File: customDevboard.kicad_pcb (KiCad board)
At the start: 4 copper layers, 40 x 40 mm, 110 parts, among them J1 Conn_01x01, J10 Conn_01x01, J11 Conn_01x01, J12 Conn_01x01, J13 Conn_01x01, J14 Conn_01x01, J15 Conn_01x01, J16 Conn_01x01, J17 Conn_01x01, J18 Conn_01x01, J19 Conn_01x01, J2 USB_C_Receptacle_USB2.0_14P, J20 From BEC, J21 Conn_01x01, J22 Conn_01x01, J23 Conn_01x01, J24 Conn_01x01, J25 PA0, J26 PA1, J27 PA7, J28 PA6, J29 PA5, J3 Conn_01x01, J30 PC1, J31 PC11, J32 PB13, J33 PA4, J34 PB2, J35 PC11, J36 PC10, J37 PB6, J38 PB7, J39 PA9, J4 Conn_01x01, J40 PA10, J41 PA2, J42 PA3, J43 PB10, J44 PB11, J5 Conn_01x01, J6 Debug, J7 To GPS, J8 BZ+, J9 COL, Q1 BC817, Q2 AO3401A, SW1 CK_KMS2xxGP, SW2 CK_KMS2xxGP, U1 DPS310, U3 TPD2EUSB30, U5 STM32F722RET6, U6 TLV75733PDRV, U7 BMI270, Y1 32.768KHz, Y2 8Mhz

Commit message: add buttons and fix drc
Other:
- board text removed: "RST"
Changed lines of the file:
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@@
-		)
-	)
-	(gr_text "RST"
-		(at 58 45 0)
-		(layer "F.SilkS")
-		(effects
-			(font
-				(size 1.5 1.5)
-				(thickness 0.3)
-				(bold yes)
-			)
-			(justify left bottom)
 		)
 	)

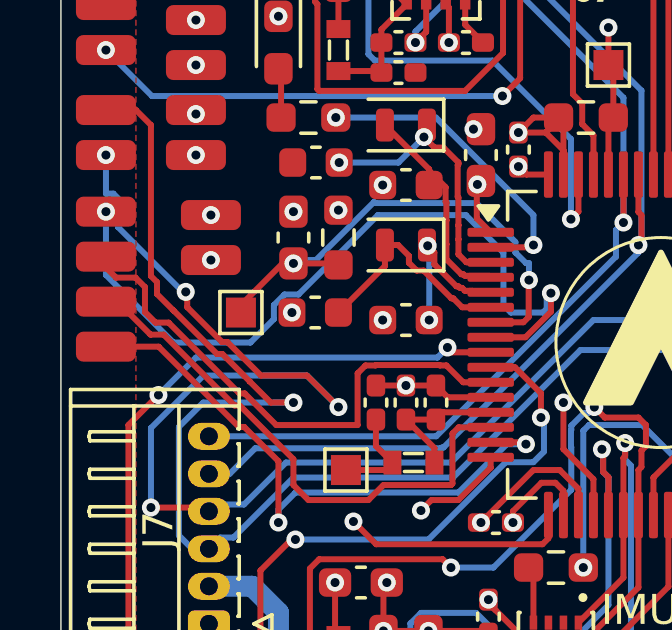
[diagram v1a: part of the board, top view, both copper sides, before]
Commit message: switch imu and barometer
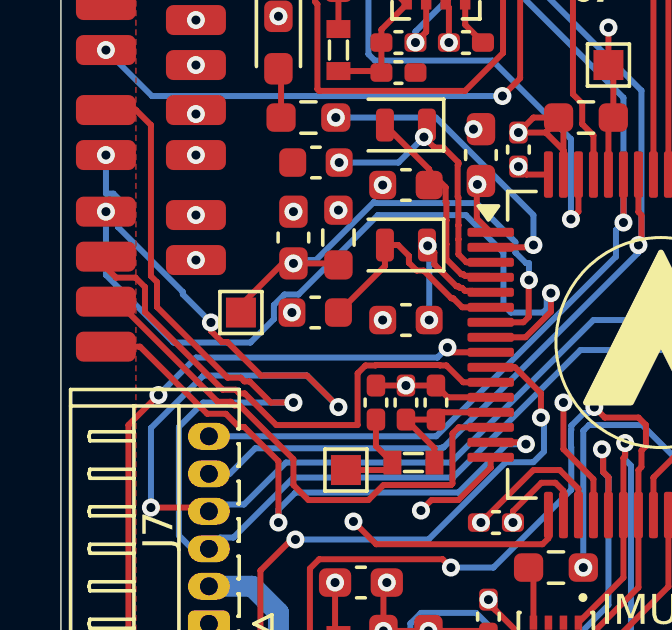
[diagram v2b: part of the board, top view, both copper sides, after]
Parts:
- moved J41 0.50 mm to (20.5, 31.8)
- moved J42 0.50 mm to (20.5, 33.2)
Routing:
- net USART2_TX: track 17.8 -> 18.3 mm

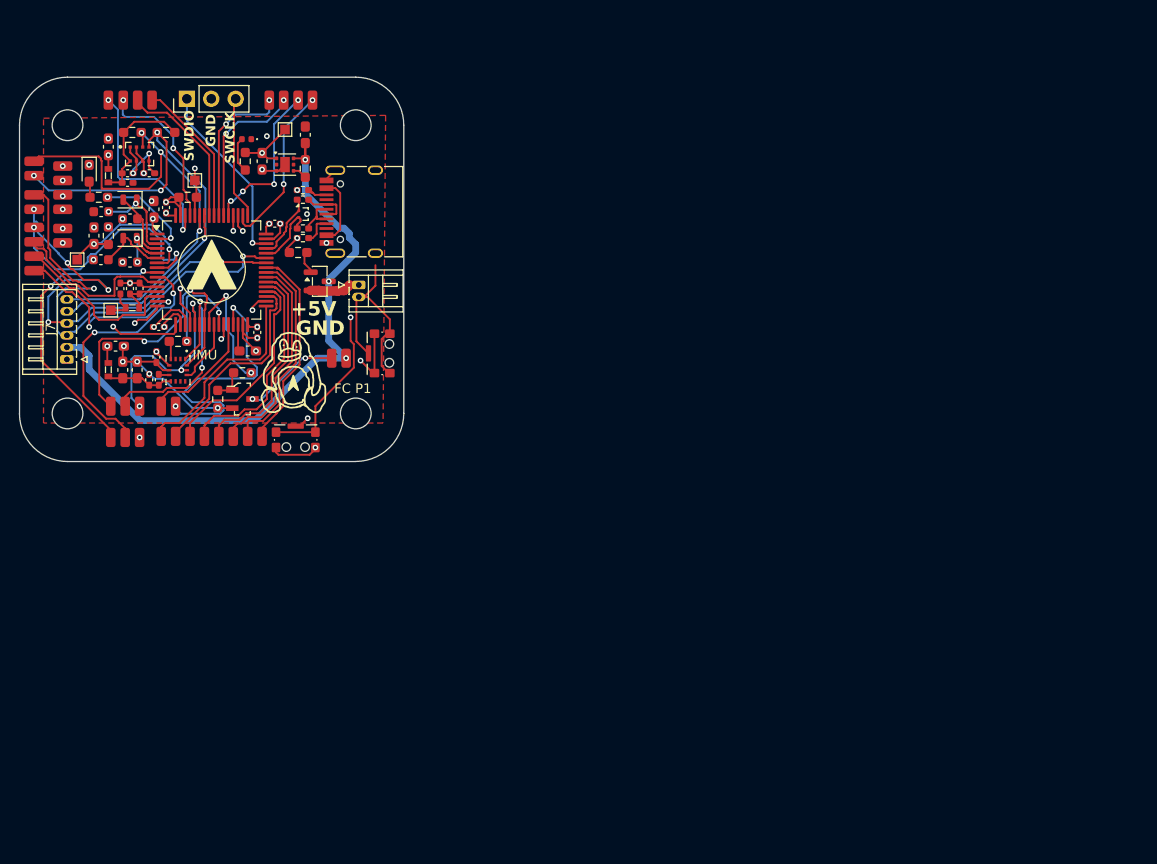
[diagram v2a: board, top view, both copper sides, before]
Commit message: restart pcb because too many new parts
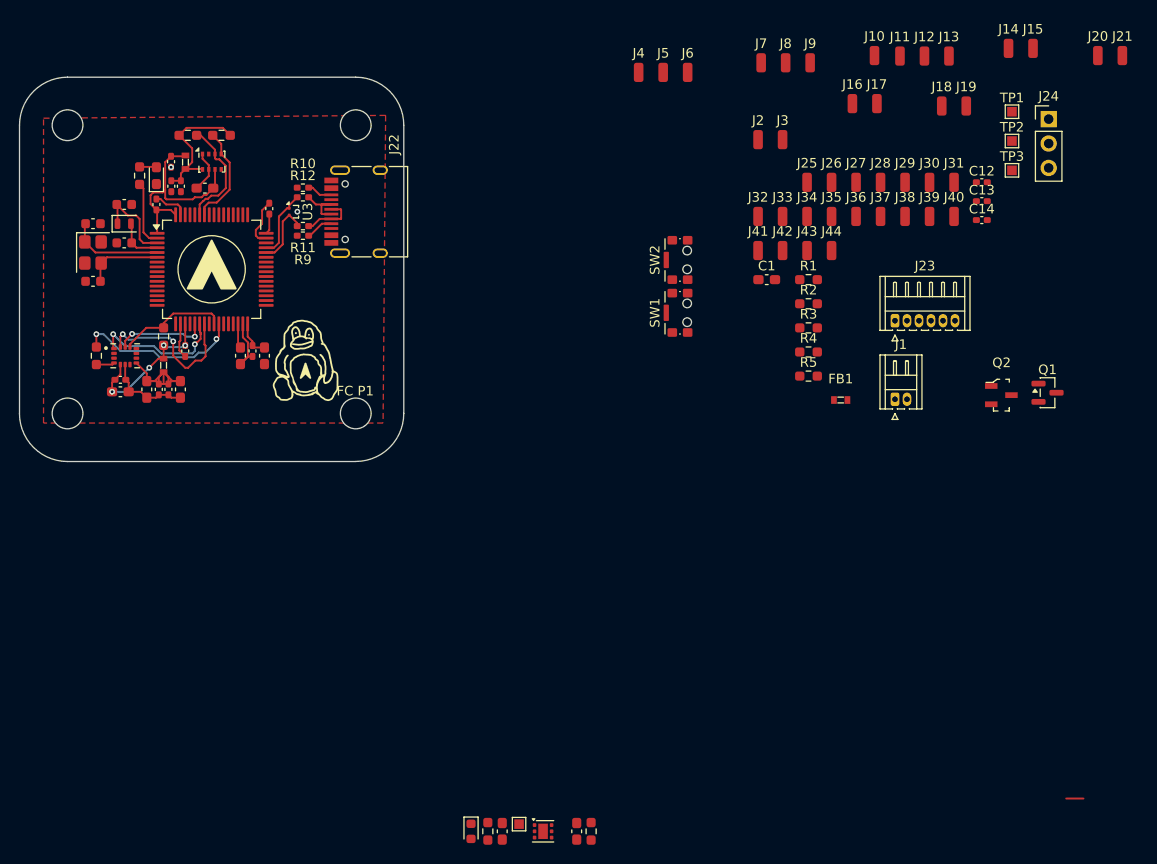
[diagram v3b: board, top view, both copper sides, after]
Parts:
- removed C27: 4.7uF, Capacitor_SMD:C_0603_1608Metric_Pad1.08x0.95mm_HandSolder
- removed C28, C36: 100nF, Capacitor_SMD:C_0603_1608Metric_Pad1.08x0.95mm_HandSolder
- removed C29: 1uF, Capacitor_SMD:C_0603_1608Metric_Pad1.08x0.95mm_HandSolder
- removed C30: 2.2uF, Capacitor_SMD:C_0603_1608Metric_Pad1.08x0.95mm_HandSolder
- removed R17: 1k, Resistor_SMD:R_0603_1608Metric_Pad0.98x0.95mm_HandSolder
- removed R18: 10k, Resistor_SMD:R_0603_1608Metric_Pad0.98x0.95mm_HandSolder
- removed R19: 1K, Resistor_SMD:R_0603_1608Metric_Pad0.98x0.95mm_HandSolder
- removed R20: 100k, Resistor_SMD:R_0603_1608Metric_Pad0.98x0.95mm_HandSolder
- removed TP5: MCU VDDA, TestPoint:TestPoint_Pad_1.0x1.0mm
- removed U6: TLV75733PDRV, Package_SON:WSON-6-1EP_2x2mm_P0.65mm_EP1x1.6mm
- removed U7: BMI270, BMI270:XDCR_BMI270
- added C14: 1uF, Capacitor_SMD:C_0402_1005Metric_Pad0.74x0.62mm_HandSolder, F.Cu at (116.2, 30.9)
- added C15: 1uF, Capacitor_SMD:C_0603_1608Metric_Pad1.08x0.95mm_HandSolder, F.Cu at (74.0, 94.5)
- added C16: 2.2uF, Capacitor_SMD:C_0603_1608Metric_Pad1.08x0.95mm_HandSolder, F.Cu at (66.2, 94.5)
- added C17: 100nF, Capacitor_SMD:C_0402_1005Metric_Pad0.74x0.62mm_HandSolder, F.Cu at (31.8, 24.8)
- added C18: 100nF, Capacitor_SMD:C_0402_1005Metric_Pad0.74x0.62mm_HandSolder, F.Cu at (30.5, 48.5)
- added R11: 27, Resistor_SMD:R_0402_1005Metric_Pad0.72x0.64mm_HandSolder, F.Cu at (45.5, 31.5)
- added R12: 27, Resistor_SMD:R_0402_1005Metric_Pad0.72x0.64mm_HandSolder, F.Cu at (45.5, 28.5)
- added R13: 10k, Resistor_SMD:R_0603_1608Metric_Pad0.98x0.95mm_HandSolder, F.Cu at (31.0, 43.0)
- added R14: 4.7k, Resistor_SMD:R_0603_1608Metric_Pad0.98x0.95mm_HandSolder, F.Cu at (37.0, 22.1)
- added R15: 4.7k, Resistor_SMD:R_0603_1608Metric_Pad0.98x0.95mm_HandSolder, F.Cu at (33.5, 22.1)
- added TP2: BOOT0, TestPoint:TestPoint_Pad_1.0x1.0mm, F.Cu at (119.3, 22.6)
- added U2: TLV75733PDRV, Package_SON:WSON-6-1EP_2x2mm_P0.65mm_EP1x1.6mm, F.Cu at (70.5, 94.5)
- added U4: ICM-42688-P, ICM_42688_P:PQFN50P300X250X97-14N, F.Cu at (27.0, 45.0)
- C1: footprint Capacitor_SMD:C_0402_1005Metric_Pad0.74x0.62mm_HandSolder -> Capacitor_SMD:C_0603_1608Metric_Pad1.08x0.95mm_HandSolder
- C10: value 10uF -> 4.7uF
- C11: value 8pF -> 10uF; footprint Capacitor_SMD:C_0603_1608Metric -> Capacitor_SMD:C_0603_1608Metric_Pad1.08x0.95mm_HandSolder
- C12: value 12.5pF -> 10nF; footprint Capacitor_SMD:C_0603_1608Metric -> Capacitor_SMD:C_0402_1005Metric_Pad0.74x0.62mm_HandSolder
- C13: value 12.5pF -> 1uF; footprint Capacitor_SMD:C_0603_1608Metric -> Capacitor_SMD:C_0402_1005Metric_Pad0.74x0.62mm_HandSolder
- C2, C5: value 1uF -> 22pF; footprint Capacitor_SMD:C_0402_1005Metric_Pad0.74x0.62mm_HandSolder -> Capacitor_SMD:C_0603_1608Metric
- C20, C21: value 100nF -> 1uF
- C24: value 10nF -> 100nF; footprint Capacitor_SMD:C_0402_1005Metric_Pad0.74x0.62mm_HandSolder -> Capacitor_SMD:C_0603_1608Metric_Pad1.08x0.95mm_HandSolder
- C25, C26: value 1uF -> 100nF; footprint Capacitor_SMD:C_0402_1005Metric_Pad0.74x0.62mm_HandSolder -> Capacitor_SMD:C_0603_1608Metric_Pad1.08x0.95mm_HandSolder
- C3: value 100nF -> 6pF; footprint Capacitor_SMD:C_0402_1005Metric_Pad0.74x0.62mm_HandSolder -> Capacitor_SMD:C_0603_1608Metric
- C7: value 100nF -> 6pF; footprint Capacitor_SMD:C_0603_1608Metric_Pad1.08x0.95mm_HandSolder -> Capacitor_SMD:C_0603_1608Metric
- C8: footprint Capacitor_SMD:C_0603_1608Metric_Pad1.08x0.95mm_HandSolder -> Capacitor_SMD:C_0402_1005Metric_Pad0.74x0.62mm_HandSolder
- C9: value 8pF -> 100nF; footprint Capacitor_SMD:C_0603_1608Metric -> Capacitor_SMD:C_0402_1005Metric_Pad0.74x0.62mm_HandSolder
- D1: value Status LED -> 3.3V LED; footprint LED_SMD:LED_0603_1608Metric_Pad1.05x0.95mm_HandSolder -> LED_SMD:LED_0603_1608Metric
- D2: value 3.3V LED -> Status LED; footprint LED_SMD:LED_0402_1005Metric -> LED_SMD:LED_0603_1608Metric_Pad1.05x0.95mm_HandSolder
- J1: value Conn_01x01 -> From BEC; footprint Connector_Wire:SolderWirePad_1x01_SMD_1x2mm -> Connector_Hirose:Hirose_DF13-02P-1.25DS_1x02_P1.25mm_Horizontal
- J10: value Conn_01x01 -> PA4
- J11: value Conn_01x01 -> PB2
- J12: value Conn_01x01 -> PC11
- J13: value Conn_01x01 -> PC10
- J14: value Conn_01x01 -> PB6
- J15: value Conn_01x01 -> PB7
- J16: value Conn_01x01 -> PA9
- J17: value Conn_01x01 -> PA10
- J18: value Conn_01x01 -> PA2
- J19: value Conn_01x01 -> PA3
- J2: value USB_C_Receptacle_USB2.0_14P -> BZ+; footprint Connector_USB:USB_C_Receptacle_HRO_TYPE-C-31-M-12 -> Connector_Wire:SolderWirePad_1x01_SMD_1x2mm
- J20: value From BEC -> PB10; footprint Connector_Hirose:Hirose_DF13-02P-1.25DS_1x02_P1.25mm_Horizontal -> Connector_Wire:SolderWirePad_1x01_SMD_1x2mm
- J21: value Conn_01x01 -> PB11
- J22: value Conn_01x01 -> USB_C_Receptacle_USB2.0_14P; footprint Connector_Wire:SolderWirePad_1x01_SMD_1x2mm -> Connector_USB:USB_C_Receptacle_HRO_TYPE-C-31-M-12
- J23: value Conn_01x01 -> To GPS; footprint Connector_Wire:SolderWirePad_1x01_SMD_1x2mm -> Connector_Hirose:Hirose_DF13-06P-1.25DS_1x06_P1.25mm_Horizontal
- J24: value Conn_01x01 -> Debug; footprint Connector_Wire:SolderWirePad_1x01_SMD_1x2mm -> Connector_PinHeader_2.54mm:PinHeader_1x03_P2.54mm_Vertical
- J25: value PA0 -> Conn_01x01
- J26: value PA1 -> Conn_01x01
- J27: value PA7 -> Conn_01x01
- J28: value PA6 -> PA0
- J29: value PA5 -> PA1
- J3: value Conn_01x01 -> COL
- J30: value PC1 -> Conn_01x01
- J31, J35: value PC11 -> Conn_01x01
- J32: value PB13 -> Conn_01x01
- J33: value PA4 -> Conn_01x01
- J34: value PB2 -> Conn_01x01
- J36: value PC10 -> Conn_01x01
- J37: value PB6 -> Conn_01x01
- J38: value PB7 -> Conn_01x01
- J39: value PA9 -> Conn_01x01
- J4: value Conn_01x01 -> PA7
- J40: value PA10 -> Conn_01x01
- J41: value PA2 -> Conn_01x01
- J42: value PA3 -> Conn_01x01
- J43: value PB10 -> Conn_01x01
- J44: value PB11 -> Conn_01x01
- J5: value Conn_01x01 -> PA6
- J6: value Debug -> PA5; footprint Connector_PinHeader_2.54mm:PinHeader_1x03_P2.54mm_Vertical -> Connector_Wire:SolderWirePad_1x01_SMD_1x2mm
- J7: value To GPS -> PC1; footprint Connector_Hirose:Hirose_DF13-06P-1.25DS_1x06_P1.25mm_Horizontal -> Connector_Wire:SolderWirePad_1x01_SMD_1x2mm
- J8: value BZ+ -> PC11
- J9: value COL -> PB13
- Q1: value BC817 -> AO3401A; footprint digikey-footprints:SOT-23-3 -> Package_TO_SOT_SMD:SOT-23
- Q2: value AO3401A -> BC817; footprint Package_TO_SOT_SMD:SOT-23 -> digikey-footprints:SOT-23-3
- R1, R2: value 4.7k -> 10k
- R10: value 100k -> 5.1k; footprint Resistor_SMD:R_0603_1608Metric_Pad0.98x0.95mm_HandSolder -> Resistor_SMD:R_0402_1005Metric_Pad0.72x0.64mm_HandSolder
- R3: value 10k -> 100k
- R4: value 10k -> 1k
- R5: value 10K -> 10k
- R6: value 5.1k -> 100k; footprint Resistor_SMD:R_0402_1005Metric_Pad0.72x0.64mm_HandSolder -> Resistor_SMD:R_0603_1608Metric_Pad0.98x0.95mm_HandSolder
- R7: value 5.1k -> 10K; footprint Resistor_SMD:R_0402_1005Metric_Pad0.72x0.64mm_HandSolder -> Resistor_SMD:R_0603_1608Metric_Pad0.98x0.95mm_HandSolder
- R8: value 27 -> 1K; footprint Resistor_SMD:R_0402_1005Metric_Pad0.72x0.64mm_HandSolder -> Resistor_SMD:R_0603_1608Metric_Pad0.98x0.95mm_HandSolder
- R9: value 27 -> 5.1k
- TP1: value BOOT0 -> NRST
- TP3: value +3.3V -> MCU VDDA
- TP4: value NRST -> +3.3V
- U1: value DPS310 -> STM32F722RET6; footprint DPS310:XDCR_DPS310 -> Package_QFP:LQFP-64_10x10mm_P0.5mm
- U5: value STM32F722RET6 -> BMP280; footprint Package_QFP:LQFP-64_10x10mm_P0.5mm -> Package_LGA:Bosch_LGA-8_2x2.5mm_P0.65mm_ClockwisePinNumbering
- Y1: value 32.768KHz -> 8MHz; footprint Crystal:Crystal_SMD_2012-2Pin_2.0x1.2mm -> Crystal:Crystal_SMD_3225-4Pin_3.2x2.5mm
- Y2: value 8Mhz -> 32.768KHz
- moved J24 106.4 mm to (123.1, 20.4), turned to 0 degrees
- moved J21 106.2 mm to (130.8, 13.8), turned to 0 degrees
- moved J40 95.8 mm to (113.3, 30.5), turned to 0 degrees
- moved J39 93.2 mm to (110.7, 30.5), turned to 0 degrees
- moved C12 91.7 mm to (116.2, 26.9), turned to 0 degrees
- moved J15 91.2 mm to (121.5, 13.0), turned to 0 degrees
- moved J38 90.9 mm to (108.2, 30.5), turned to 0 degrees
- moved J31 90.3 mm to (113.3, 26.9)
- moved J23 90.2 mm to (107.1, 41.3), turned to 0 degrees
- moved J30 89.3 mm to (110.7, 26.9)
- moved C13 88.7 mm to (116.2, 28.9), turned to 0 degrees
- moved J37 88.2 mm to (105.6, 30.5), turned to 0 degrees
- moved J19 87.8 mm to (114.5, 19.0), turned to 0 degrees
- moved J1 87.6 mm to (107.1, 49.5)
- moved J14 87.6 mm to (119.0, 13.0), turned to 0 degrees
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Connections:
- C1 pad 1: Net-(U7-VDD) -> NRST
- C10 pad 1: Net-(U7-VDD) -> Net-(U1-VCAP_1)
- C11 pad 1: Net-(U5-PH1) -> +3.3V
- C12 pad 1: Net-(U5-PC14) -> Net-(U1-VDDA)
- C13 pad 1: Net-(U5-PC15) -> Net-(U1-VDDA)
- C19 pad 1: +3.3V -> Net-(U5-VDD)
- C2 pad 1: Net-(U7-VDD) -> Net-(U1-PH0)
- C20 pad 1: +3.3V -> Net-(U4-VDD)
- C21 pad 1: +3.3V -> Net-(U5-VDD)
- C23 pad 1: +3.3V -> Net-(U4-VDD)
- C24 pad 1: Net-(U5-VDDA) -> Net-(U4-VDD)
- C25 pad 1: Net-(U5-VDDA) -> +3.3V
- C26 pad 1: +3.3VA -> +3.3V
- C3 pad 1: +3.3V -> Net-(U1-PC14)
- C4 pad 1: Net-(U1-VDD) -> +3.3V
- C5 pad 1: Net-(U1-VDD) -> Net-(U1-PH1)
- C7 pad 1: +3.3V -> Net-(U1-PC15)
- C8 pad 1: Net-(U7-VDD) -> +3.3V
- C9 pad 1: Net-(U5-PH0) -> +3.3V
- FB1 pad 1: Net-(U5-VDDA) -> Net-(U1-VDDA)
- FB2 pad 2: Net-(U1-VDD) -> Net-(U5-VDD)
- FB3 pad 2: Net-(U7-VDD) -> Net-(U4-VDD)
- J1 pad 1: PB9 -> Net-(J1-Pin_1)
- J10 pad 1: PB3 -> SPI3_NSS
- J11 pad 1: PD2 -> SPI3_MOSI
- J12 pad 1: PC12 -> SPI3_MISO
- J13 pad 1: PA15 -> SPI3_SCK
- J14 pad 1: PA8 -> I2C1_SCL
- J15 pad 1: PC9 -> I2C1_SDA
- J16 pad 1: PC8 -> USART1_TX
- J17 pad 1: PC7 -> USART1_RX
- J18 pad 1: PC6 -> USART2_TX
- J19 pad 1: PB15 -> USART2_RX
- J20 pad 1: Net-(J20-Pin_1) -> USART3_TX
- J21 pad 1: PB14 -> USART3_RX
- J23 pad 1: PC0 -> GND
- J24 pad 1: PC3 -> SYS_JTMS-SWDIO
- J25 pad 1: PA0 -> PB9
- J26 pad 1: PA1 -> PC0
- J27 pad 1: SPI1_MOSI -> PC3
- J28 pad 1: SPI1_MISO -> PA0
- J29 pad 1: SPI1_SCK -> PA1
- J3 pad 1: PB8 -> Net-(J3-Pin_1)
- J30 pad 1: SPI2_MOSI -> PB8
- J31 pad 1: SPI2_MISO -> PB5
- J32 pad 1: SPI2_SCK -> PB4
- J33 pad 1: SPI3_NSS -> PB3
- J34 pad 1: SPI3_MOSI -> PD2
- J35 pad 1: SPI3_MISO -> PC12
- J36 pad 1: SPI3_SCK -> PA8
- J37 pad 1: I2C1_SCL -> PC9
- J38 pad 1: I2C1_SDA -> PC8
- J39 pad 1: USART1_TX -> PC7
- J4 pad 1: PB5 -> SPI1_MOSI
- J40 pad 1: USART1_RX -> PC6
- J41 pad 1: USART2_TX -> PB15
- J42 pad 1: USART2_RX -> PB14
- J43 pad 1: USART3_TX -> PB12
- J44 pad 1: USART3_RX -> PA15
- J5 pad 1: PB4 -> SPI1_MISO
- J6 pad 1: SYS_JTMS-SWDIO -> SPI1_SCK
- J7 pad 1: GND -> SPI2_MOSI
- J8 pad 1: +5V -> SPI2_MISO
- J9 pad 1: Net-(J9-Pin_1) -> SPI2_SCK
- Q1 pad 1: Net-(Q1-B) -> Net-(Q1-G)
- Q1 pad 2: GND -> Net-(J1-Pin_1)
- Q1 pad 3: Net-(J9-Pin_1) -> +5V
- Q2 pad 1: Net-(Q2-G) -> Net-(Q2-B)
- Q2 pad 2: Net-(J20-Pin_1) -> GND
- Q2 pad 3: +5V -> Net-(J3-Pin_1)
- R1 pad 1: Net-(U1-VDD) -> +3.3V
- R1 pad 2: I2C1_SDA -> NRST
- R10 pad 1: Net-(U6-EN) -> GND
- R10 pad 2: +5V -> Net-(J22-CC2)
- R2 pad 1: Net-(U1-VDD) -> BOOT0
- R2 pad 2: I2C1_SCL -> GND
- R3 pad 1: BOOT0 -> Net-(Q1-G)
- R4 pad 1: +3.3V -> Beeper
- R4 pad 2: NRST -> Net-(Q2-B)
- R5 pad 1: +3.3V -> Net-(Q2-B)
- R5 pad 2: Net-(D2-A) -> GND
- R6 pad 1: Net-(J2-CC1) -> Net-(U2-EN)
- R6 pad 2: GND -> +5V
- R7 pad 1: GND -> +3.3V
- R7 pad 2: Net-(J2-CC2) -> Net-(D1-A)
- R8 pad 1: Net-(J2-D--PadA7) -> Status_LED
- R8 pad 2: USB_D- -> Net-(D2-A)
- R9 pad 1: USB_D+ -> Net-(J22-CC1)
- R9 pad 2: Net-(J2-D+-PadA6) -> GND
- TP1 pad 1: BOOT0 -> NRST
- TP3 pad 1: +3.3V -> +3.3VA
- TP4 pad 1: NRST -> +3.3V
- U1 pad 1: GND -> +3.3V
- U1 pad 2: +3.3V -> Status_LED
- U1 pad 3: I2C1_SDA -> Net-(U1-PC14)
- U1 pad 4: I2C1_SCL -> Net-(U1-PC15)
- U1 pad 5: GND -> Net-(U1-PH0)
- U1 pad 6: +3.3V -> Net-(U1-PH1)
- U1 pad 7: GND -> NRST
- U1 pad 8: Net-(U1-VDD) -> PC0
- U5 pad 1: +3.3V -> GND
- U5 pad 2: Status_LED -> unconnected-(U5-CSB-Pad2)
- U5 pad 3: Net-(U5-PC14) -> I2C1_SDA
- U5 pad 4: Net-(U5-PC15) -> I2C1_SCL
- U5 pad 5: Net-(U5-PH0) -> unconnected-(U5-SDO-Pad5)
- U5 pad 6: Net-(U5-PH1) -> +3.3V
- U5 pad 7: NRST -> GND
- U5 pad 8: PC0 -> Net-(U5-VDD)
- Y1 pad 1: Net-(U5-PC14) -> Net-(U1-PH0)
- Y1 pad 2: Net-(U5-PC15) -> GND
- Y2 pad 1: Net-(U5-PH0) -> Net-(U1-PC14)
- Y2 pad 2: Net-(U5-PH1) -> Net-(U1-PC15)
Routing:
- net +5V: track 65.1 -> 0.00 mm, vias 3 -> 0
- net NRST: track 48.4 -> 0.00 mm, vias 3 -> 0
- net USART1_TX: track 48.4 -> 0.00 mm, vias 5 -> 0
- net GND: track 79.8 -> 32.0 mm, vias 27 -> 2
- net USART1_RX: track 47.5 -> 0.00 mm, vias 2 -> 0
- net BOOT0: track 45.8 -> 0.00 mm, vias 2 -> 0
- net I2C1_SCL: track 55.6 -> 10.6 mm, vias 4 -> 0
- net I2C1_SDA: track 52.9 -> 11.7 mm, vias 3 -> 0
- net SPI2_MOSI: track 31.0 -> 0.00 mm, vias 2 -> 0
- net USART3_RX: track 29.1 -> 0.00 mm, vias 2 -> 0
- net SPI3_MOSI: track 27.7 -> 0.00 mm, vias 2 -> 0
- net SPI2_MISO: track 27.4 -> 0.00 mm, vias 2 -> 0
- net PC0: track 25.5 -> 0.00 mm, vias 2 -> 0
- net SPI3_SCK: track 23.4 -> 0.00 mm, vias 2 -> 0
- net PC6: track 22.7 -> 0.00 mm
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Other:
- board text removed: "+5V"
- board text removed: "GND"
- board text removed: "IMU"
- board text removed: "SWCLK"
- board text removed: "SWDIO"

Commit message: ready for ship
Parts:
- J23: value To GPS -> SWDIO; footprint Connector_Hirose:Hirose_DF13-06P-1.25DS_1x06_P1.25mm_Horizontal -> Connector_Wire:SolderWirePad_1x01_SMD_1x2mm
- J24: value Debug -> SWCLK; footprint Connector_PinHeader_2.54mm:PinHeader_1x03_P2.54mm_Vertical -> Connector_Wire:SolderWirePad_1x01_SMD_1x2mm
- SW1, SW2: value CK_KMS2xxGP -> SW_SPST; footprint Button_Switch_SMD:SW_SPST_CK_KMS2xxGP -> Button_Switch_SMD:SW_SPST_B3U-3000P
- TP1, TP2, TP3, TP4: moved to B.Cu
- moved J21 109.5 mm to (22.2, 28.0), turned to -90 degrees
- moved J20 106.8 mm to (22.2, 26.5), turned to -90 degrees
- moved J13 95.8 mm to (18.5, 31.0), turned to -90 degrees
- moved J15 94.9 mm to (26.8, 18.5), turned to 180 degrees
- moved J24 94.9 mm to (28.2, 22.2)
- moved J12 93.0 mm to (18.5, 29.5), turned to -90 degrees
- moved J19 92.9 mm to (28.2, 53.5)
- moved TP3 92.5 mm to (27.8, 38.5)
- moved J18 92.0 mm to (26.8, 53.5)
- moved J14 90.9 mm to (28.2, 18.5), turned to 180 degrees
- moved J11 90.3 mm to (18.5, 28.0), turned to -90 degrees
- moved J29 90.3 mm to (18.5, 37.2), turned to -90 degrees
- moved C12 89.5 mm to (27.8, 40.8), turned to 180 degrees
- moved C13 89.1 mm to (27.8, 39.8), turned to 180 degrees
- moved C14 88.6 mm to (27.8, 37.2)
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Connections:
- J23 pad 1: GND -> SYS_JTMS-SWDIO
- J24 pad 1: SYS_JTMS-SWDIO -> SYS_JTCK-SWCLK
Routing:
- net +5V: track 0.00 -> 37.9 mm, vias 0 -> 3
- net SPI2_SCK: track 0.00 -> 32.7 mm, vias 0 -> 2
- net NRST: track 0.00 -> 31.9 mm, vias 0 -> 2
- net SPI3_MISO: track 0.00 -> 28.4 mm, vias 0 -> 2
- net PC6: track 0.00 -> 28.2 mm, vias 0 -> 2
- net SPI3_MOSI: track 0.00 -> 27.0 mm, vias 0 -> 2
- net USART3_TX: track 0.00 -> 26.8 mm, vias 0 -> 2
- net BOOT0: track 0.00 -> 26.8 mm, vias 0 -> 2
- net +3.3V: track 43.9 -> 70.3 mm, vias 4 -> 11
- net USART3_RX: track 0.00 -> 25.9 mm, vias 0 -> 4
- net PA8: track 0.00 -> 25.7 mm, vias 0 -> 2
- net SPI3_SCK: track 0.00 -> 25.7 mm, vias 0 -> 2
- net SPI3_NSS: track 0.00 -> 25.6 mm, vias 0 -> 2
- net PB15: track 0.00 -> 25.1 mm, vias 0 -> 2
- net GND: track 32.0 -> 56.6 mm, vias 2 -> 18
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
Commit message: it came to me in a dream
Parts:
- moved U4 0.45 mm to (25.8, 44.5), turned to 90 degrees
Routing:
- net SPI1_SCK: track 26.0 -> 19.1 mm
- net SPI_CS_IMU1: track 20.1 -> 17.3 mm
- net Net-(U4-VDD): track 28.7 -> 31.0 mm
- net SPI1_MOSI: track 33.1 -> 31.3 mm
- net Net-(U4-INT1/INT): track 1.86 -> 0.25 mm
- net SPI1_MISO: track 24.9 -> 23.4 mm
- net +3.3V: track 70.3 -> 71.5 mm
- net GND: track 56.6 -> 57.3 mm

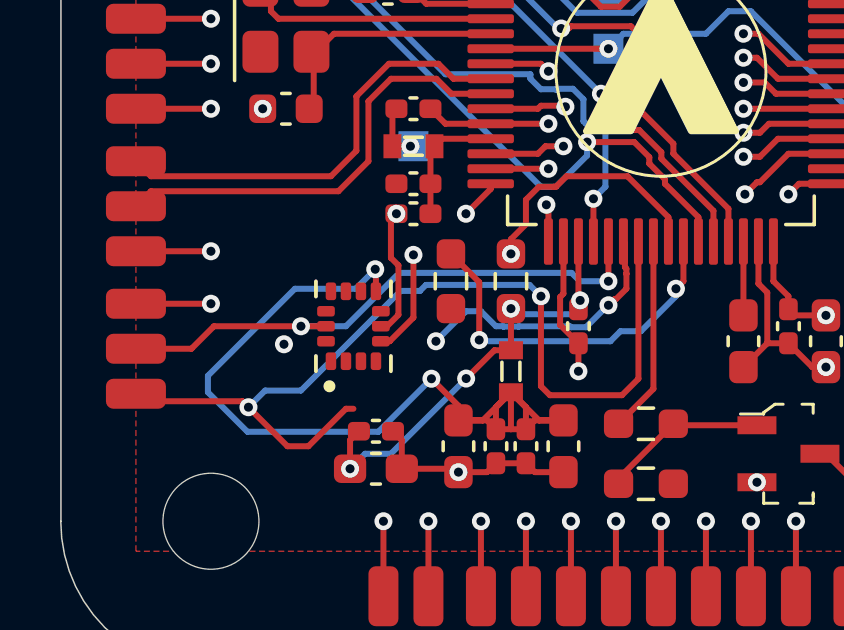
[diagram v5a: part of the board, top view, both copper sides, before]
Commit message: add ground plane
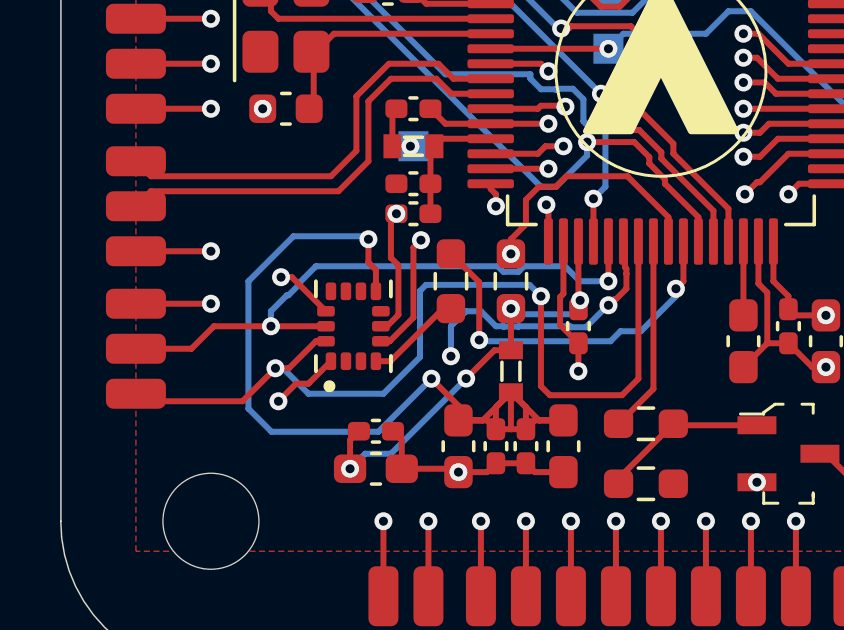
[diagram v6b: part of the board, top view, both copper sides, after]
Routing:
- net +3.3V: track 71.5 -> 80.7 mm
- net Net-(U4-INT1/INT): track 0.25 -> 3.47 mm
- net SPI_CS_IMU1: track 17.3 -> 19.6 mm
- net SPI1_MISO: track 23.4 -> 25.4 mm, vias 3 -> 4
- net SPI1_SCK: track 19.1 -> 20.7 mm
- net Net-(U4-VDD): track 31.0 -> 31.8 mm
- net USART2_RX: track 16.7 -> 17.5 mm
- net SPI1_MOSI: track 31.3 -> 30.6 mm

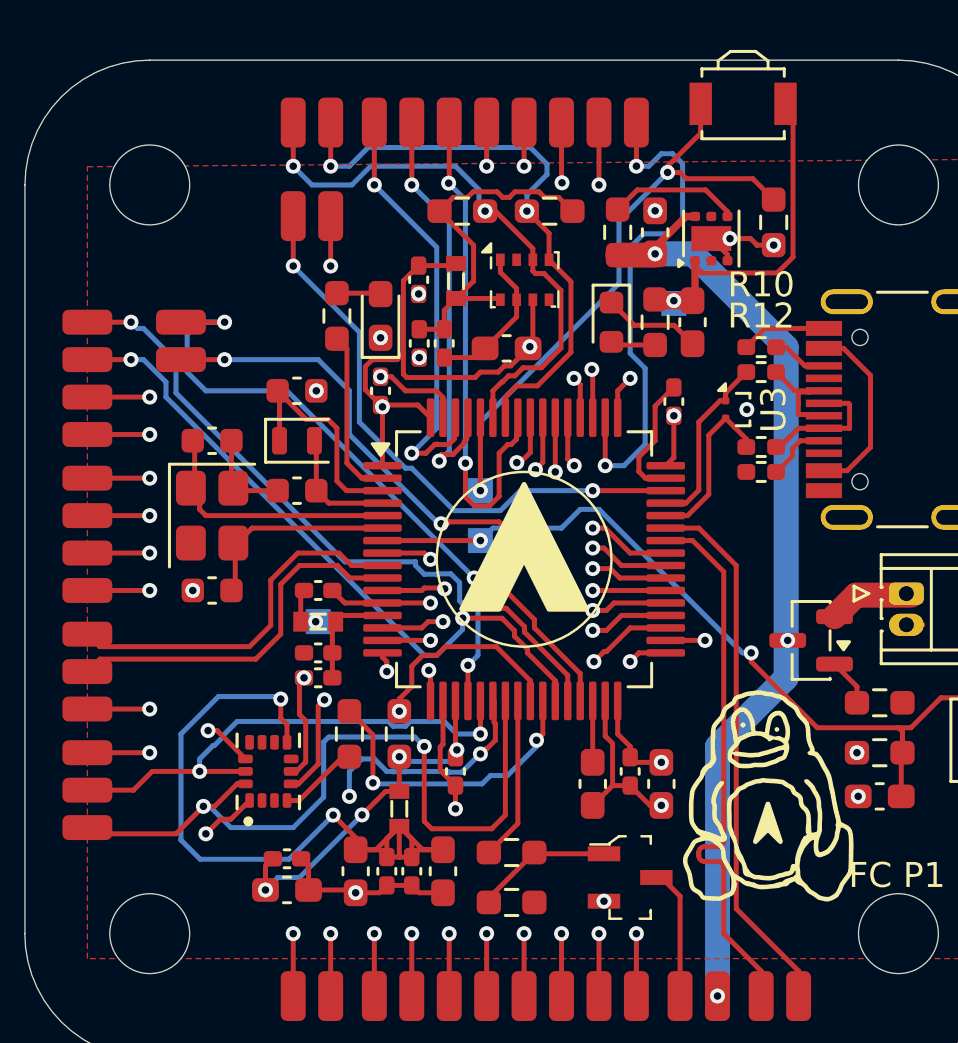
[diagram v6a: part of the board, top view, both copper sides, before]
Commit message: beef up power traces
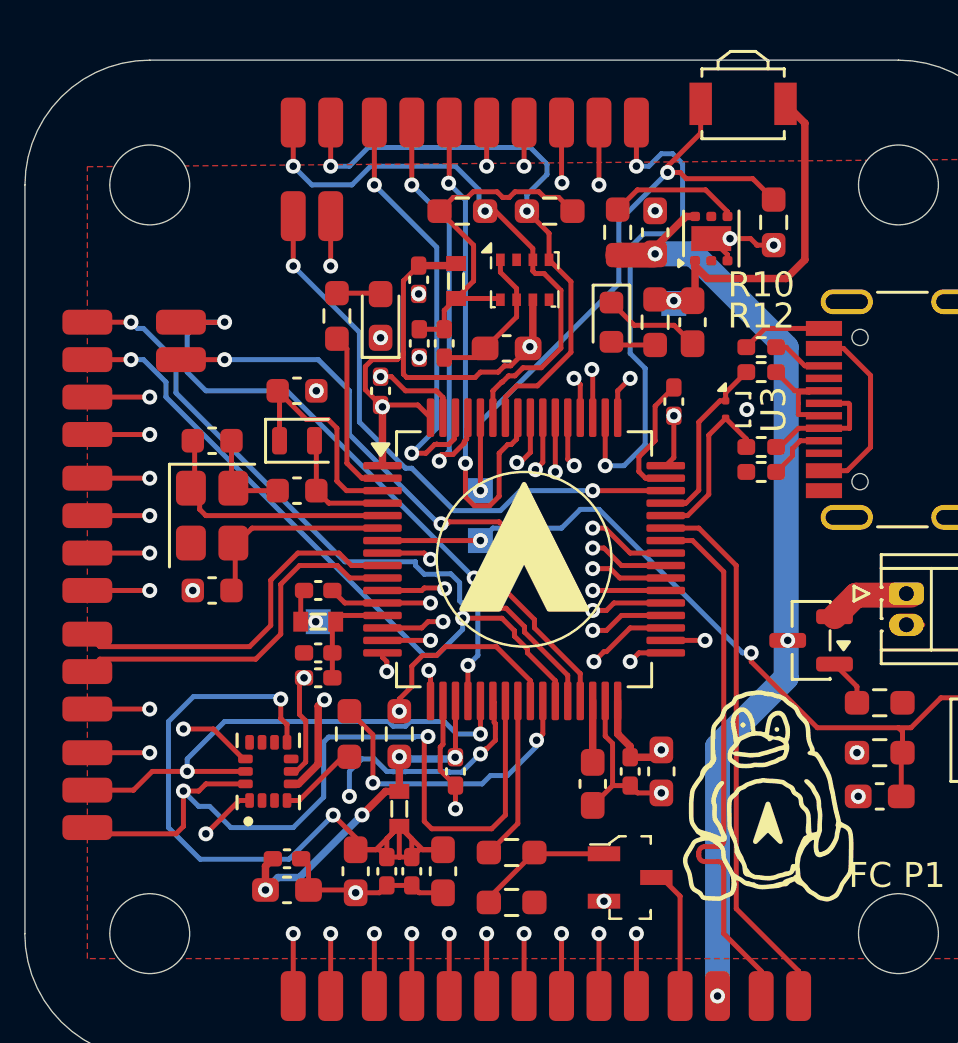
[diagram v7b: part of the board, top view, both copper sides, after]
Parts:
- moved C11 0.50 mm to (41.5, 44.5)
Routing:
- net SPI1_MOSI: track 30.6 -> 32.9 mm
- net SPI_CS_IMU1: track 19.6 -> 21.6 mm
- net +3.3V: track 80.7 -> 81.8 mm
- net Net-(U4-VDD): track 31.8 -> 32.8 mm
